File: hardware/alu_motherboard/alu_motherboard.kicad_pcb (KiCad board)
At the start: 2 copper layers, 45 x 284 mm, 85 parts, among them J1 OUT, J3 ADD_SUB, J4 BITOPS, J5 SHIFT, J6 IN, Q1 IRLML6244, Q2 IRLML6244, Q3 IRLML6244, Q4 IRLML6244, Q5 IRLML6244, Q6 IRLML6244, Q7 IRLML6244, Q8 IRLML6244, U1 74HC00, U10 74HC00, U11 74HC00, U12 74HC00, U13 74HC00, U14 74HC00, U15 74HC00, U16 74HC00, U17 74HC00, U18 74HC00, U19 74HC00, U2 74HC00, U20 74HC00, U21 74HC00, U3 74HC00, U4 74HC00, U5 74HC00, U53 74HC00, U6 74HC00, U7 74HC00, U8 74HC00, U9 74HC00

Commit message: fixed schematic of ALU motherboard
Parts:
- removed J1: OUT, Connector_PinHeader_2.54mm:PinHeader_2x15_P2.54mm_Horizontal
- removed J6: IN, Connector_PinHeader_2.54mm:PinHeader_2x15_P2.54mm_Horizontal
- added J2: Conn_02x26_Odd_Even, Connector_PinHeader_2.54mm:PinHeader_2x26_P2.54mm_Horizontal, F.Cu at (155.5, 0.85)
- Q3, Q4, Q5, Q6: footprint Package_TO_SOT_SMD:SOT-23-3 -> Package_TO_SOT_SMD:SOT-23_Handsoldering
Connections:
- D1 pad 2: /RES0 -> /RES7
- D2 pad 2: /RES1 -> /RES6
- D3 pad 2: /RES2 -> /RES5
- D4 pad 2: /RES3 -> /RES4
- D5 pad 2: /RES4 -> /RES3
- D6 pad 2: /RES5 -> /RES2
- D7 pad 2: /RES6 -> /RES1
- D8 pad 2: /RES7 -> /RES0
- J3 pad 41: /A0 -> /B7
- J4 pad 20: /A0 -> /B7

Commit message: finished schematic and draft of ALU motherboard
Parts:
- removed U53: 74HC00, Package_SO:SOIC-14_3.9x8.7mm_P1.27mm
- added D13: LED, LED_SMD:LED_0603_1608Metric_Pad1.05x0.95mm_HandSolder, F.Cu at (183.9, 7.00)
- added D14: LED, LED_SMD:LED_0603_1608Metric_Pad1.05x0.95mm_HandSolder, F.Cu at (180.3, 7.00)
- added D15: LED, LED_SMD:LED_0603_1608Metric_Pad1.05x0.95mm_HandSolder, F.Cu at (176.7, 7.00)
- added D16: LED, LED_SMD:LED_0603_1608Metric_Pad1.05x0.95mm_HandSolder, F.Cu at (173.2, 7.00)
- added D17: LED, LED_SMD:LED_0603_1608Metric_Pad1.05x0.95mm_HandSolder, F.Cu at (169.6, 7.00)
- added D18: LED, LED_SMD:LED_0603_1608Metric_Pad1.05x0.95mm_HandSolder, F.Cu at (166.1, 7.00)
- added D19: LED, LED_SMD:LED_0603_1608Metric_Pad1.05x0.95mm_HandSolder, F.Cu at (162.5, 7.00)
- added D20: LED, LED_SMD:LED_0603_1608Metric_Pad1.05x0.95mm_HandSolder, F.Cu at (159.0, 7.00)
- added Q10: IRLML6244, Package_TO_SOT_SMD:SOT-23-3, F.Cu at (180.2, 11.8)
- added Q11: IRLML6244, Package_TO_SOT_SMD:SOT-23-3, F.Cu at (176.7, 11.8)
- added Q12: IRLML6244, Package_TO_SOT_SMD:SOT-23-3, F.Cu at (173.1, 11.8)
- added Q13: IRLML6244, Package_TO_SOT_SMD:SOT-23-3, F.Cu at (169.6, 11.8)
- added Q14: IRLML6244, Package_TO_SOT_SMD:SOT-23-3, F.Cu at (166.0, 11.8)
- added Q15: IRLML6244, Package_TO_SOT_SMD:SOT-23-3, F.Cu at (162.4, 11.8)
- added Q16: IRLML6244, Package_TO_SOT_SMD:SOT-23-3, F.Cu at (158.9, 11.8)
- added Q9: IRLML6244, Package_TO_SOT_SMD:SOT-23-3, F.Cu at (183.8, 11.8)
- added R12: 1000, Resistor_SMD:R_0603_1608Metric_Pad0.98x0.95mm_HandSolder, F.Cu at (183.9, 8.60)
- added R13: 1000, Resistor_SMD:R_0603_1608Metric_Pad0.98x0.95mm_HandSolder, F.Cu at (180.3, 8.60)
- added R14: 1000, Resistor_SMD:R_0603_1608Metric_Pad0.98x0.95mm_HandSolder, F.Cu at (176.7, 8.60)
- added R15: 1000, Resistor_SMD:R_0603_1608Metric_Pad0.98x0.95mm_HandSolder, F.Cu at (173.2, 8.60)
- added R16: 1000, Resistor_SMD:R_0603_1608Metric_Pad0.98x0.95mm_HandSolder, F.Cu at (169.6, 8.60)
- added R17: 1000, Resistor_SMD:R_0603_1608Metric_Pad0.98x0.95mm_HandSolder, F.Cu at (166.1, 8.60)
- added R18: 1000, Resistor_SMD:R_0603_1608Metric_Pad0.98x0.95mm_HandSolder, F.Cu at (162.5, 8.60)
- added R19: 1000, Resistor_SMD:R_0603_1608Metric_Pad0.98x0.95mm_HandSolder, F.Cu at (159.0, 8.60)
- Q3, Q4, Q5, Q6: footprint Package_TO_SOT_SMD:SOT-23_Handsoldering -> Package_TO_SOT_SMD:SOT-23-3
- moved C23 333.7 mm to (189.5, -67.0), turned to 90 degrees
- moved C14 328.6 mm to (167.1, 37.4), turned to 90 degrees
- moved C15 327.8 mm to (167.1, 20.6), turned to 90 degrees
- moved C22 324.5 mm to (182.9, -67.0), turned to 90 degrees
- moved C16 324.2 mm to (167.1, 29.0), turned to 90 degrees
- moved C13 322.1 mm to (167.1, 45.9), turned to 90 degrees
- moved C18 319.9 mm to (167.0, -70.4), turned to -90 degrees
- moved C12 315.8 mm to (167.1, 54.3), turned to 90 degrees
- moved U14 311.3 mm to (161.6, 37.5), turned to -90 degrees
- moved C3 309.8 mm to (167.1, 62.7), turned to 90 degrees
- moved U15 309.5 mm to (161.6, 29.1), turned to -90 degrees
- moved Q6 308.5 mm to (179.8, 1.64), turned to 90 degrees
- moved U16 308.2 mm to (161.6, 20.6), turned to -90 degrees
- moved C2 304.0 mm to (167.1, 71.1), turned to 90 degrees
- moved Q3 303.3 mm to (183.8, 1.64), turned to 90 degrees
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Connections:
- net /8Bit_Mux1/A0 renamed /MRES0
- net /8Bit_Mux1/A1 renamed /MRES1
- net /8Bit_Mux1/A2 renamed /MRES2
- net /8Bit_Mux1/A3 renamed /MRES3
- net /8Bit_Mux1/A4 renamed /MRES4
- net /8Bit_Mux1/A5 renamed /MRES5
- net /8Bit_Mux1/A6 renamed /MRES6
- net /8Bit_Mux1/A7 renamed /MRES7
- net /ASS renamed /AASS
- net /B0 renamed /ABY0
- net /B1 renamed /ABY1
- net /B2 renamed /ABY2
- net /SOB renamed /ASOB
- D1 pad 2: /RES7 -> /ORES7
- D2 pad 2: /RES6 -> /ORES6
- D3 pad 2: /RES5 -> /ORES5
- D4 pad 2: /RES4 -> /ORES4
- D5 pad 2: /RES3 -> /ORES3
- D6 pad 2: /RES2 -> /ORES2
- D7 pad 2: /RES1 -> /ORES1
- D8 pad 2: /RES0 -> /ORES0
- J2 pad 24: /RES0 -> /ORES0
- J2 pad 26: /RES1 -> /ORES1
- J2 pad 28: /RES2 -> /ORES2
- J2 pad 30: /RES3 -> /ORES3
- J2 pad 34: /RES4 -> /ORES4
- J2 pad 36: /RES5 -> /ORES5
- J2 pad 38: /RES6 -> /ORES6
- J2 pad 40: /RES7 -> /ORES7
- J2 pad 41: /OP1 -> /BS1
- J3 pad 10: /RES3 -> /ARES3
- J3 pad 14: /RES4 -> /ARES4
- J3 pad 16: /RES5 -> /ARES5
- J3 pad 18: /RES6 -> /ARES6
- J3 pad 20: /RES7 -> /ARES7
- J3 pad 34: /OVF -> /AOVF
- J3 pad 36: /COUT -> /ACOUT
- J3 pad 4: /RES0 -> /ARES0
- J3 pad 42: /CIN -> /ACIN
- J3 pad 6: /RES1 -> /ARES1
- J3 pad 8: /RES2 -> /ARES2
- J4 pad 10: /RES7 -> /BRES7
- J4 pad 3: /RES0 -> /BRES0
- J4 pad 37: /OP1 -> /BS1
- J4 pad 4: /RES1 -> /BRES1
- J4 pad 5: /RES2 -> /BRES2
- J4 pad 6: /RES3 -> /BRES3
- J4 pad 7: /RES4 -> /BRES4
- J4 pad 8: /RES5 -> /BRES5
- J4 pad 9: /RES6 -> /BRES6
- J5 pad 10: /RES7 -> /SRES7
- J5 pad 3: /RES0 -> /SRES0
- J5 pad 4: /RES1 -> /SRES1
- J5 pad 5: /RES2 -> /SRES2
- J5 pad 6: /RES3 -> /SRES3
- J5 pad 7: /RES4 -> /SRES4
- J5 pad 8: /RES5 -> /SRES5
- J5 pad 9: /RES6 -> /SRES6
- Q6 pad 1: /RES7 -> /8Bit_Mux1/RES7
- R9 pad 2: /OP1 -> /BS1
- U1 pad 1: /RES0 -> /BRES0
- U1 pad 6: /RES0 -> /8Bit_Mux1/RES0
- U10 pad 1: /RES1 -> /BRES1
- U10 pad 6: /RES1 -> /8Bit_Mux1/RES1
- U11 pad 1: /RES2 -> /BRES2
- U11 pad 6: /RES2 -> /8Bit_Mux1/RES2
- U12 pad 1: /RES3 -> /BRES3
- U12 pad 6: /RES3 -> /8Bit_Mux1/RES3
- U13 pad 1: /RES4 -> /BRES4
- U13 pad 6: /RES4 -> /8Bit_Mux1/RES4
- U14 pad 1: /RES5 -> /BRES5
- U14 pad 6: /RES5 -> /8Bit_Mux1/RES5
- U15 pad 1: /RES6 -> /BRES6
- U15 pad 6: /RES6 -> /8Bit_Mux1/RES6
- U16 pad 1: /RES7 -> /BRES7
- U16 pad 6: /RES7 -> /8Bit_Mux1/RES7
- U17 pad 1: /RES3 -> /SRES3
- U17 pad 9: /RES3 -> /ARES3
- U18 pad 1: /RES4 -> /SRES4
- U18 pad 9: /RES4 -> /ARES4
- U19 pad 1: /RES5 -> /SRES5
- U19 pad 9: /RES5 -> /ARES5
- U2 pad 1: /OP1 -> /BS1
- U2 pad 10: /OP1 -> /BS1
- U2 pad 2: /OP1 -> /BS1
- U2 pad 5: /COUT -> /ACOUT
- U20 pad 1: /RES6 -> /SRES6
- U20 pad 9: /RES6 -> /ARES6
- U21 pad 1: /RES7 -> /SRES7
- U21 pad 9: /RES7 -> /ARES7
- U4 pad 5: /OVF -> /AOVF
- U5 pad 1: /OP1 -> /OP2
- U5 pad 2: /OP1 -> /OP2
- U5 pad 4: /OP2 -> /BS1
- U5 pad 5: /OP2 -> /BS1
- U6 pad 1: (no net) -> /CEN
- U6 pad 2: (no net) -> /CIN
- U6 pad 3: (no net) -> Net-(U6-Pad3)
- U6 pad 4: Net-(U53-Pad3) -> Net-(U6-Pad3)
- U6 pad 5: Net-(U53-Pad3) -> Net-(U6-Pad3)
- U6 pad 6: /CIN -> /ACIN
- U7 pad 1: /RES0 -> /SRES0
- U7 pad 9: /RES0 -> /ARES0
- U8 pad 1: /RES1 -> /SRES1
- U8 pad 9: /RES1 -> /ARES1
- U9 pad 1: /RES2 -> /SRES2
- U9 pad 9: /RES2 -> /ARES2
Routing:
- net +5V: track 0.00 -> 822.2 mm, vias 0 -> 47
- net /BS1: track 0.00 -> 310.9 mm, vias 0 -> 9
- net /ABY0: track 0.00 -> 256.9 mm, vias 0 -> 4
- net /AASS: track 0.00 -> 256.5 mm, vias 0 -> 3
- net /ABY1: track 0.00 -> 247.2 mm, vias 0 -> 4
- net /ABY2: track 0.00 -> 246.2 mm, vias 0 -> 4
- net /A6: track 0.00 -> 240.2 mm, vias 0 -> 3
- net /A7: track 0.00 -> 238.9 mm, vias 0 -> 3
- net /A0: track 0.00 -> 236.6 mm, vias 0 -> 3
- net /A4: track 0.00 -> 233.5 mm, vias 0 -> 3
- net /A2: track 0.00 -> 233.1 mm, vias 0 -> 3
- net /A5: track 0.00 -> 231.4 mm, vias 0 -> 3
- net /A1: track 0.00 -> 229.7 mm, vias 0 -> 2
- net /ARES0: track 0.00 -> 227.8 mm, vias 0 -> 3
- net /A3: track 0.00 -> 226.4 mm, vias 0 -> 3
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- added copper zone on F.Cu, net +5V
- added copper zone on B.Cu, net GND
- added copper zone on In1.Cu, net GND
- added copper zone on In2.Cu, net GND
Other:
- board size 45 x 284 mm -> 40 x 284 mm
- copper layers 2 -> 4

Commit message: feedback to ALU motherboard PCB
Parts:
- added H1: MountingHole_Pad, MountingHole:MountingHole_2.2mm_M2_Pad, F.Cu at (204.3, 337.0)
- added H2: MountingHole_Pad, MountingHole:MountingHole_2.2mm_M2_Pad, F.Cu at (175.3, 337.0)
- added H3: MountingHole_Pad, MountingHole:MountingHole_2.2mm_M2_Pad, F.Cu at (175.3, 64.0)
- added H4: MountingHole_Pad, MountingHole:MountingHole_2.2mm_M2_Pad, F.Cu at (204.3, 64.0)
- moved C22 164.0 mm to (192.7, 96.7), turned to 180 degrees
- moved C23 157.2 mm to (192.7, 90.2), turned to 180 degrees
- moved D20 142.4 mm to (199.7, 143.5)
- moved R19 142.4 mm to (199.7, 145.1)
- moved Q16 142.4 mm to (199.6, 148.3)
- moved D19 140.6 mm to (196.1, 143.5)
- moved Q15 140.6 mm to (196.0, 148.3)
- moved R18 140.6 mm to (196.1, 145.1)
- moved D18 139.0 mm to (192.5, 143.5)
- moved Q14 139.0 mm to (192.5, 148.3)
- moved R17 139.0 mm to (192.5, 145.1)
- moved D17 137.9 mm to (189.0, 143.5)
- moved Q13 137.9 mm to (188.9, 148.3)
- moved R16 137.9 mm to (189.0, 145.1)
- moved C10 137.4 mm to (182.9, 267.8)
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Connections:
- net /ABY0 renamed /B0
- net /ABY1 renamed /B1
- net /ABY2 renamed /B2
- net /ASOB renamed /SSOB
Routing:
- net +5V: track 822.2 -> 799.5 mm
- net /8Bit_Mux1/RES7: track 57.3 -> 76.1 mm
- net /8Bit_Mux1/RES6: track 23.2 -> 40.8 mm
- net /8Bit_Mux1/RES0: track 89.6 -> 75.1 mm
- net /ORES7: track 167.7 -> 181.4 mm, vias 2 -> 4
- net /8Bit_Mux1/RES1: track 78.4 -> 65.5 mm
- net /ORES6: track 162.4 -> 173.7 mm, vias 2 -> 4
- net /8Bit_Mux1/RES5: track 34.4 -> 45.0 mm
- net /8Bit_Mux1/RES2: track 67.4 -> 57.3 mm
- net /ORES4: track 160.4 -> 168.3 mm, vias 2 -> 4
- net /ORES1: track 163.0 -> 155.8 mm, vias 2 -> 4
- net /ORES5: track 160.5 -> 167.4 mm, vias 2 -> 4
- net /ORES0: track 167.0 -> 160.4 mm, vias 2 -> 4
- net /ORES3: track 158.3 -> 154.0 mm, vias 2 -> 3
- net /8Bit_Mux1/RES3: track 56.6 -> 53.0 mm
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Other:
- board text added: "A0"
- board text added: "A1"
- board text added: "A2"
- board text added: "A3"
- board text added: "A4"
- board text added: "A5"
- board text added: "A6"
- board text added: "A7"
- board text added: "ALU Motherboard | Rev 1.0"
- board text added: "ASS"
- board text added: "B0"
- board text added: "B1"
- board text added: "B2"
- board text added: "B3"
- board text added: "B4"
- board text added: "B5"
- board text added: "B6"
- board text added: "B7"
- board text added: "BY0"
- board text added: "BY1"
- board text added: "BY2"
- board text added: "C"
- board text added: "CEN"
- board text added: "CIN"
- board text added: "COUT"
- board text added: "DIR"
- board text added: "FLAG"
- board text added: "GND"
- board text added: "N"
- board text added: "NEG"
- board text added: "OP0"
- board text added: "OP1"
- board text added: "OP2"
- board text added: "OVF"
- board text added: "RES"
- board text added: "RES0"
- board text added: "RES1"
- board text added: "RES2"
- board text added: "RES3"
- board text added: "RES4"
- board text added: "RES5"
- board text added: "RES6"
- board text added: "RES7"
- board text added: "SEL0"
- board text added: "SEL1"
- board text added: "SOB"
- board text added: "V"
- board text added: "VCC"
- board text added: "Z"
- board text added: "ZERO"
- board text added: "mrab"

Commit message: more ALU motherboard feedback
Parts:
- added D21: LED, LED_SMD:LED_0603_1608Metric_Pad1.05x0.95mm_HandSolder, F.Cu at (187.9, 124.6)
- added R20: 1000, Resistor_SMD:R_0603_1608Metric_Pad0.98x0.95mm_HandSolder, F.Cu at (187.9, 126.2)
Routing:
- net +5V: track 799.5 -> 802.9 mm
- net Net-(D21-K): track 0.00 -> 1.63 mm
- net GND: track 176.4 -> 177.7 mm, vias 764 -> 765
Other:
- board text added: "&&"
- board text added: "+/-"
- board text added: "0"
- board text added: "1"
- board text added: "2"
- board text added: "3"
- board text added: "4"
- board text added: "5"
- board text added: "6"
- board text added: "7"
- board text added: ">>"
- board text added: "PWR"

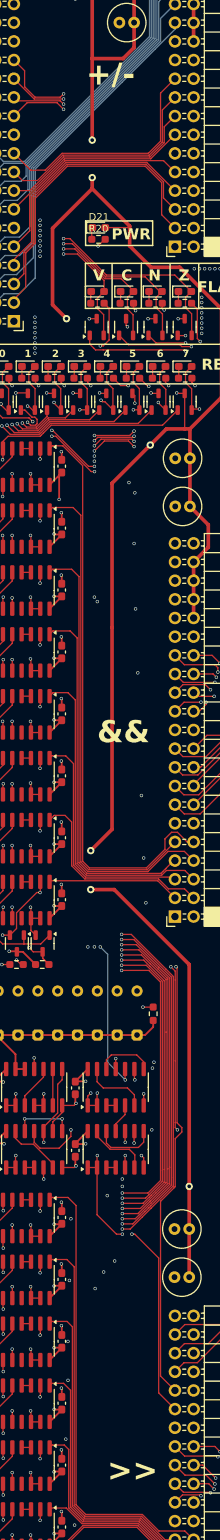
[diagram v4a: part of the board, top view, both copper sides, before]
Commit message: added PWR indicator to alu_shift
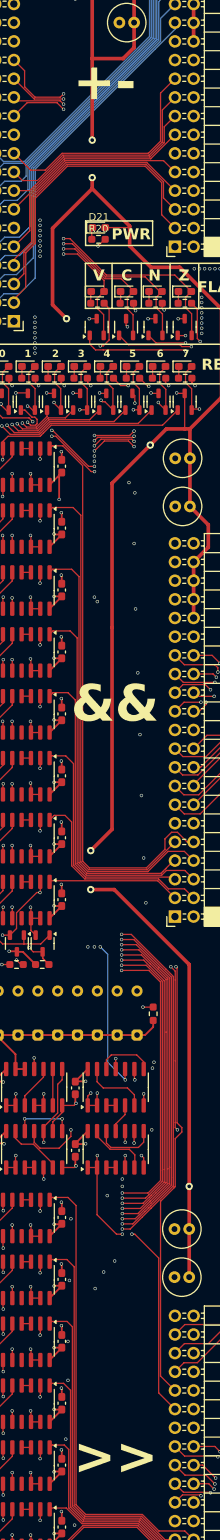
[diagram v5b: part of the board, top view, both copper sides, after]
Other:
- board text added: "+-"
- board text removed: "+/-"
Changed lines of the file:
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@@
+		(layer "B.SilkS")
+	)
+	(gr_rect
+		(start 188 72.4)
+		(end 202.2 128.8)
+		(stroke
+			(width 0.2)
+			(type default)
+		)
+		(fill none)
 		(layer "B.SilkS")
 	)
@@
 		)
 	)
-	(gr_text "+/-"
-		(at 189.5 103.75 0)
+	(gr_text "+-"
+		(at 188.7 104.8 0)
 		(layer "F.SilkS")
 		(effects
 			(font
-				(size 3 3)
-				(thickness 0.75)
+				(size 5 5)
+				(thickness 1.25)
 				(bold yes)
 			)
@@
 	)
 	(gr_text ">>"
-		(at 192.5 293.75 0)
+		(at 190.2 291.9 0)
 		(layer "F.SilkS")
 		(effects
 			(font
-				(size 3 3)
-				(thickness 0.75)
+				(size 5 5)
+				(thickness 1.25)
 				(bold yes)
 			)
@@
 	)
 	(gr_text "&&"
-		(at 191.25 193.25 0)
+		(at 190.1 189.4 0)
 		(layer "F.SilkS")
 		(effects
 			(font
-				(size 3 3)
-				(thickness 0.75)
-				(bold yes)
-			)
+				(size 5 5)
+				(thickness 1.25)
+				(bold yes)
+			)

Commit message: fixed mux include
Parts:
- C1, C2, C3, C4, C5, C6: value 330nF -> 100uF; footprint Capacitor_SMD:C_0603_1608Metric_Pad1.08x0.95mm_HandSolder -> Capacitor_THT:C_Radial_D5.0mm_H11.0mm_P2.00mm
- C22, C23, C24, C25, C26, C27: value 100uF -> 330nF; footprint Capacitor_THT:C_Radial_D5.0mm_H11.0mm_P2.00mm -> Capacitor_SMD:C_0603_1608Metric_Pad1.08x0.95mm_HandSolder
- D1, D2, D3, D4, D5: value D_Schottky -> LED; footprint Library:DO35_Packed -> LED_SMD:LED_0603_1608Metric_Pad1.05x0.95mm_HandSolder
- D10, D11, D12, D13, D9: value LED -> D_Schottky; footprint LED_SMD:LED_0603_1608Metric_Pad1.05x0.95mm_HandSolder -> Library:DO35_Packed
- moved U6 252.5 mm to (177.4, 318.4), turned to -90 degrees
- moved R17 182.7 mm to (176.6, 327.1)
- moved R11 182.5 mm to (189.0, 145.1)
- moved R10 182.1 mm to (185.4, 145.1)
- moved R15 182.1 mm to (180.2, 327.1)
- moved R16 179.7 mm to (173.7, 324.1), turned to -90 degrees
- moved R9 179.2 mm to (181.9, 145.1), turned to 0 degrees
- moved Q14 176.7 mm to (176.7, 324.3), turned to -90 degrees
- moved Q8 176.2 mm to (185.4, 148.3), turned to 90 degrees
- moved Q13 176.2 mm to (180.3, 324.3), turned to -90 degrees
- moved Q7 176.0 mm to (181.8, 148.3), turned to 90 degrees
- moved C24 156.7 mm to (182.9, 318.3), turned to 90 degrees
- moved C4 156.7 mm to (200.3, 162.6), turned to 180 degrees
- moved U1 150.4 mm to (188.3, 66.1), turned to 90 degrees
- moved C1 119.8 mm to (192.7, 96.7), turned to 180 degrees
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- renumbered J3 to J1, J4 to J3, J5 to J4
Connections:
- D1 pad 2: /ORES7 -> +5V
- D10 pad 2: /COUT -> /ORES4
- D11 pad 1: Net-(D11-K) -> Net-(D10-K)
- D11 pad 2: /OVF -> /ORES5
- D12 pad 1: Net-(D12-K) -> Net-(D10-K)
- D12 pad 2: /NEG -> /ORES6
- D13 pad 1: Net-(D13-K) -> Net-(D10-K)
- D13 pad 2: /ORES0 -> /ORES7
- D14 pad 2: /ORES1 -> /ORES0
- D15 pad 2: /ORES2 -> /ORES1
- D16 pad 2: /ORES3 -> /ORES2
- D17 pad 2: /ORES4 -> /ORES3
- D18 pad 2: /ORES5 -> /ORES4
- D19 pad 2: /ORES6 -> /ORES5
- D2 pad 1: Net-(D1-K) -> Net-(D2-K)
- D2 pad 2: /ORES6 -> /COUT
- D20 pad 2: /ORES7 -> /ORES6
- D21 pad 2: +5V -> /ORES7
- D3 pad 1: Net-(D1-K) -> Net-(D3-K)
- D3 pad 2: /ORES5 -> /OVF
- D4 pad 1: Net-(D1-K) -> Net-(D4-K)
- D4 pad 2: /ORES4 -> /ZERO
- D5 pad 1: Net-(D1-K) -> Net-(D5-K)
- D5 pad 2: /ORES3 -> /NEG
- D6 pad 1: Net-(D1-K) -> Net-(D10-K)
- D6 pad 2: /ORES2 -> /ORES0
- D7 pad 1: Net-(D1-K) -> Net-(D10-K)
- D8 pad 1: Net-(D1-K) -> Net-(D10-K)
- D8 pad 2: /ORES0 -> /ORES2
- D9 pad 1: Net-(D9-K) -> Net-(D10-K)
- D9 pad 2: /ZERO -> /ORES3
- Q1 pad 2: GND -> /COUT
- Q1 pad 3: Net-(Q1-D) -> +5V
- Q10 pad 1: /8Bit_Mux1/RES1 -> /8Bit_Mux3/RES5
- Q10 pad 2: /ORES1 -> /ORES5
- Q11 pad 1: /8Bit_Mux1/RES2 -> /8Bit_Mux3/RES6
- Q11 pad 2: /ORES2 -> /ORES6
- Q12 pad 1: /8Bit_Mux1/RES3 -> /8Bit_Mux3/RES7
- Q12 pad 2: /ORES3 -> /ORES7
- Q13 pad 1: /8Bit_Mux1/RES4 -> Net-(Q13-G)
- Q13 pad 2: /ORES4 -> GND
- Q13 pad 3: +5V -> Net-(Q13-D)
- Q14 pad 1: /8Bit_Mux1/RES5 -> Net-(Q13-G)
- Q14 pad 2: /ORES5 -> Net-(Q14-S)
- Q15 pad 1: /8Bit_Mux1/RES6 -> Net-(Q15-G)
- Q15 pad 2: /ORES6 -> GND
- Q15 pad 3: +5V -> Net-(Q15-D)
- Q16 pad 1: /8Bit_Mux1/RES7 -> Net-(Q15-G)
- Q16 pad 2: /ORES7 -> Net-(Q16-S)
- Q2 pad 1: Net-(Q1-G) -> Net-(Q2-G)
- Q2 pad 2: Net-(Q2-S) -> /OVF
- Q4 pad 1: Net-(Q4-G) -> /8Bit_Mux3/RES7
- Q4 pad 2: /COUT -> /NEG
- Q5 pad 1: Net-(Q5-G) -> /8Bit_Mux3/RES0
- Q5 pad 2: /OVF -> /ORES0
- Q6 pad 1: /8Bit_Mux1/RES7 -> /8Bit_Mux3/RES1
- Q6 pad 2: /NEG -> /ORES1
- Q7 pad 1: Net-(Q7-G) -> /8Bit_Mux3/RES2
- Q7 pad 2: GND -> /ORES2
- Q7 pad 3: Net-(Q7-D) -> +5V
- Q8 pad 1: Net-(Q7-G) -> /8Bit_Mux3/RES3
- Q8 pad 2: Net-(Q8-S) -> /ORES3
- Q9 pad 1: /8Bit_Mux1/RES0 -> /8Bit_Mux3/RES4
- Q9 pad 2: /ORES0 -> /ORES4
- R1 pad 1: Net-(Q1-G) -> Net-(D1-K)
- R1 pad 2: /OP2 -> GND
- R10 pad 1: +5V -> Net-(D17-K)
- R10 pad 2: Net-(Q7-D) -> GND
- R11 pad 1: Net-(Q8-S) -> Net-(D18-K)
- R12 pad 1: Net-(D13-K) -> Net-(D19-K)
- R13 pad 1: Net-(D14-K) -> Net-(D20-K)
- R14 pad 1: Net-(D15-K) -> Net-(D21-K)
- R15 pad 1: Net-(D16-K) -> +5V
- R15 pad 2: GND -> Net-(Q13-D)
- R16 pad 1: Net-(D17-K) -> Net-(Q13-G)
- R16 pad 2: GND -> /BS1
- R17 pad 1: Net-(D18-K) -> Net-(Q14-S)
- R18 pad 1: Net-(D19-K) -> +5V
- R18 pad 2: GND -> Net-(Q15-D)
- R19 pad 1: Net-(D20-K) -> Net-(Q15-G)
- R19 pad 2: GND -> /OP2
- R2 pad 1: +5V -> Net-(D2-K)
- R2 pad 2: Net-(Q1-D) -> GND
- R20 pad 1: Net-(D21-K) -> Net-(Q16-S)
- R3 pad 1: Net-(Q2-S) -> Net-(D3-K)
- R4 pad 1: Net-(D1-K) -> Net-(D4-K)
- R5 pad 1: Net-(D9-K) -> Net-(D5-K)
- R7 pad 1: Net-(D11-K) -> Net-(D14-K)
- R8 pad 1: Net-(D12-K) -> Net-(D15-K)
- R9 pad 1: Net-(Q7-G) -> Net-(D16-K)
- R9 pad 2: /BS1 -> GND
- U1 pad 1: /BRES0 -> /CEN
- U1 pad 10: Net-(Q1-D) -> GND
- U1 pad 2: Net-(Q2-S) -> /CIN
- U1 pad 5: Net-(U1-Pad5) -> Net-(U1-Pad3)
- U1 pad 6: /8Bit_Mux1/RES0 -> /ACIN
- U1 pad 8: Net-(U1-Pad5) -> unconnected-(U1-Pad8)
- U1 pad 9: /MRES0 -> GND
- U10 pad 1: /BRES1 -> /SRES4
- U10 pad 10: Net-(Q1-D) -> Net-(Q13-D)
- U10 pad 2: Net-(Q2-S) -> Net-(Q14-S)
- U10 pad 6: /8Bit_Mux1/RES1 -> /MRES4
- U10 pad 9: /MRES1 -> /ARES4
- U11 pad 1: /BRES2 -> /SRES5
- U11 pad 10: Net-(Q1-D) -> Net-(Q13-D)
- U11 pad 2: Net-(Q2-S) -> Net-(Q14-S)
- U11 pad 6: /8Bit_Mux1/RES2 -> /MRES5
- U11 pad 9: /MRES2 -> /ARES5
- U12 pad 1: /BRES3 -> /SRES6
- U12 pad 10: Net-(Q1-D) -> Net-(Q13-D)
- U12 pad 2: Net-(Q2-S) -> Net-(Q14-S)
- U12 pad 6: /8Bit_Mux1/RES3 -> /MRES6
- U12 pad 9: /MRES3 -> /ARES6
- U13 pad 1: /BRES4 -> /SRES7
- U13 pad 10: Net-(Q1-D) -> Net-(Q13-D)
- U13 pad 2: Net-(Q2-S) -> Net-(Q14-S)
- U13 pad 6: /8Bit_Mux1/RES4 -> /MRES7
- U13 pad 9: /MRES4 -> /ARES7
- U14 pad 1: /BRES5 -> /BRES0
- U14 pad 10: Net-(Q1-D) -> Net-(Q15-D)
- U14 pad 2: Net-(Q2-S) -> Net-(Q16-S)
- U14 pad 6: /8Bit_Mux1/RES5 -> /8Bit_Mux3/RES0
- U14 pad 9: /MRES5 -> /MRES0
- U15 pad 1: /BRES6 -> /BRES1
- U15 pad 10: Net-(Q1-D) -> Net-(Q15-D)
- U15 pad 2: Net-(Q2-S) -> Net-(Q16-S)
- U15 pad 6: /8Bit_Mux1/RES6 -> /8Bit_Mux3/RES1
- U15 pad 9: /MRES6 -> /MRES1
- U16 pad 1: /BRES7 -> /BRES2
- U16 pad 10: Net-(Q1-D) -> Net-(Q15-D)
- U16 pad 2: Net-(Q2-S) -> Net-(Q16-S)
- U16 pad 6: /8Bit_Mux1/RES7 -> /8Bit_Mux3/RES2
- U16 pad 9: /MRES7 -> /MRES2
- U17 pad 1: /SRES3 -> /BRES3
- U17 pad 10: Net-(Q7-D) -> Net-(Q15-D)
- U17 pad 2: Net-(Q8-S) -> Net-(Q16-S)
- U17 pad 6: /MRES3 -> /8Bit_Mux3/RES3
- U17 pad 9: /ARES3 -> /MRES3
- U18 pad 1: /SRES4 -> /BRES4
- U18 pad 10: Net-(Q7-D) -> Net-(Q15-D)
- U18 pad 2: Net-(Q8-S) -> Net-(Q16-S)
- U18 pad 6: /MRES4 -> /8Bit_Mux3/RES4
- U18 pad 9: /ARES4 -> /MRES4
- U19 pad 1: /SRES5 -> /BRES5
- U19 pad 10: Net-(Q7-D) -> Net-(Q15-D)
- U19 pad 2: Net-(Q8-S) -> Net-(Q16-S)
- U19 pad 6: /MRES5 -> /8Bit_Mux3/RES5
- U19 pad 9: /ARES5 -> /MRES5
- U20 pad 1: /SRES6 -> /BRES6
- U20 pad 10: Net-(Q7-D) -> Net-(Q15-D)
- U20 pad 2: Net-(Q8-S) -> Net-(Q16-S)
- U20 pad 6: /MRES6 -> /8Bit_Mux3/RES6
- U20 pad 9: /ARES6 -> /MRES6
- U21 pad 1: /SRES7 -> /BRES7
- U21 pad 10: Net-(Q7-D) -> Net-(Q15-D)
- U21 pad 2: Net-(Q8-S) -> Net-(Q16-S)
- U21 pad 6: /MRES7 -> /8Bit_Mux3/RES7
- U21 pad 9: /ARES7 -> /MRES7
- U3 pad 11: Net-(Q4-G) -> Net-(Q1-G)
- U4 pad 11: Net-(Q5-G) -> Net-(Q2-G)
- U5 pad 12: Net-(D1-K) -> Net-(D10-K)
- U5 pad 13: Net-(D1-K) -> Net-(D10-K)
- U6 pad 1: /CEN -> /SRES0
- U6 pad 10: GND -> Net-(Q13-D)
- U6 pad 2: /CIN -> Net-(Q14-S)
- U6 pad 5: Net-(U6-Pad3) -> Net-(U6-Pad5)
- U6 pad 6: /ACIN -> /MRES0
- U6 pad 8: unconnected-(U6-Pad8) -> Net-(U6-Pad5)
- U6 pad 9: GND -> /ARES0
- U7 pad 1: /SRES0 -> /SRES1
- U7 pad 10: Net-(Q7-D) -> Net-(Q13-D)
- U7 pad 2: Net-(Q8-S) -> Net-(Q14-S)
- U7 pad 6: /MRES0 -> /MRES1
- U7 pad 9: /ARES0 -> /ARES1
- U8 pad 1: /SRES1 -> /SRES2
- U8 pad 10: Net-(Q7-D) -> Net-(Q13-D)
- U8 pad 2: Net-(Q8-S) -> Net-(Q14-S)
- U8 pad 6: /MRES1 -> /MRES2
- U8 pad 9: /ARES1 -> /ARES2
- U9 pad 1: /SRES2 -> /SRES3
- U9 pad 10: Net-(Q7-D) -> Net-(Q13-D)
- U9 pad 2: Net-(Q8-S) -> Net-(Q14-S)
- U9 pad 6: /MRES2 -> /MRES3
- U9 pad 9: /ARES2 -> /ARES3
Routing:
- net Net-(Q2-G): track 0.00 -> 151.8 mm, vias 0 -> 3
- net Net-(Q5-G): track 146.7 -> 0.00 mm, vias 3 -> 0
- net Net-(Q4-G): track 121.7 -> 0.00 mm, vias 3 -> 0
- net Net-(Q1-G): track 9.67 -> 127.5 mm, vias 0 -> 3
- net Net-(Q7-D): track 86.1 -> 0.00 mm, vias 9 -> 0
- net Net-(Q13-D): track 0.00 -> 86.1 mm, vias 0 -> 9
- net Net-(Q2-S): track 85.3 -> 0.00 mm, vias 10 -> 0
- net Net-(Q16-S): track 0.00 -> 85.3 mm, vias 0 -> 10
- net Net-(Q15-D): track 0.00 -> 84.0 mm, vias 0 -> 9
- net Net-(Q1-D): track 84.0 -> 0.00 mm, vias 9 -> 0
- net Net-(Q8-S): track 83.9 -> 0.00 mm, vias 10 -> 0
- net Net-(Q14-S): track 0.00 -> 83.9 mm, vias 0 -> 10
- net /8Bit_Mux3/RES7: track 0.00 -> 82.1 mm, vias 0 -> 3
- net /8Bit_Mux1/RES7: track 76.1 -> 0.00 mm, vias 3 -> 0
- net /8Bit_Mux3/RES0: track 0.00 -> 75.1 mm, vias 0 -> 2
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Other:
- board text removed: "&&"
- board text removed: "+-"
- board text removed: ">>"
